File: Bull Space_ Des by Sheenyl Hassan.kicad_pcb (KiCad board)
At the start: 2 copper layers, 45 x 77 mm, 36 parts, among them IC1 TEENSY_4.0, IC2 XB24CZ7PIT-004, J1 Screw_Terminal_01x06, Q1 AOI21357, Q2 2N7002, Q3 2N7002, Q4 2N7002, Q5 AOI21357, U1 VXO7803-1000, U2 Flight-Computer_Adafruit_GPS_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

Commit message: Checked Parts
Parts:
- moved D1 3.98 mm to (91.3, 66.8)
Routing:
- net Net-(D1-Pad4): track 12.3 -> 16.7 mm
- net LED-R: track 30.9 -> 35.1 mm
- net LED-G: track 31.5 -> 35.7 mm
- net LED-B: track 32.1 -> 36.3 mm
- net Net-(D1-Pad2): track 12.0 -> 15.1 mm
- net Net-(D1-Pad3): track 14.5 -> 17.5 mm
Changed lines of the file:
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@@
   )
   (footprint "LED_THT:LED_D5.0mm-4_RGB_Staggered_Pins" (layer "F.Cu")
-    (at 95.16 67.61)
+    (at 91.26 66.81)
     (descr "LED, diameter 5.0mm, 4 pins, WP154A4, https://www.kingbright.com/attachments/file/psearch/000/00/00/L-154A4SUREQBFZGEW(Ver.11A).pdf")
     (tags "rgb led")
@@
   (gr_line (start 72 64) (end 72 141) (layer "Edge.Cuts") (width 0.1))
   (gr_line (start 116.75 141) (end 72 141) (layer "Edge.Cuts") (width 0.1))
-  (segment (start 109.098 74.214) (end 106.304 71.42) (width 0.25) (layer "F.Cu") (net 1))
-  (segment (start 109.098 75.3335) (end 109.098 74.214) (width 0.25) (layer "F.Cu") (net 1))
-  (segment (start 106.304 71.42) (end 102.272 71.42) (width 0.25) (layer "F.Cu") (net 1))
-  (segment (start 102.272 71.42) (end 99.986 69.134) (width 0.25) (layer "F.Cu") (net 1))
-  (segment (start 107.16 73.292) (end 105.796 71.928) (width 0.25) (layer "F.Cu") (net 2))
-  (segment (start 105.796 71.928) (end 100.462 71.928) (width 0.25) (layer "F.Cu") (net 2))
-  (segment (start 100.462 71.928) (end 98.462 69.928) (width 0.25) (layer "F.Cu") (net 2))
-  (segment (start 107.16 75.3335) (end 107.16 73.292) (width 0.25) (layer "F.Cu") (net 2))
-  (segment (start 98.462 69.928) (end 98.462 67.61) (width 0.25) (layer "F.Cu") (net 2))
-  (segment (start 105.26 73.424) (end 104.272 72.436) (width 0.25) (layer "F.Cu") (net 3))
-  (segment (start 104.272 72.436) (end 100.24 72.436) (width 0.25) (layer "F.Cu") (net 3))
-  (segment (start 105.26 75.3335) (end 105.26 73.424) (width 0.25) (layer "F.Cu") (net 3))
-  (segment (start 100.24 72.436) (end 96.938 69.134) (width 0.25) (layer "F.Cu") (net 3))
+  (segment (start 96.086 68.334) (end 96.086 69.606792) (width 0.25) (layer "F.Cu") (net 1))
+  (segment (start 96.086 69.606792) (end 96.744829 70.265621) (width 0.25) (layer "F.Cu") (net 1))
+  (segment (start 104.030121 70.265621) (end 109.098 75.3335) (width 0.25) (layer "F.Cu") (net 1))
+  (segment (start 96.744829 70.265621) (end 104.030121 70.265621) (width 0.25) (layer "F.Cu") (net 1))
+  (segment (start 94.562 66.81) (end 94.562 69.222282) (width 0.25) (layer "F.Cu") (net 2))
+  (segment (start 96.054859 70.715141) (end 102.541641 70.715141) (width 0.25) (layer "F.Cu") (net 2))
+  (segment (start 102.541641 70.715141) (end 107.16 75.3335) (width 0.25) (layer "F.Cu") (net 2))
+  (segment (start 94.562 69.222282) (end 96.054859 70.715141) (width 0.25) (layer "F.Cu") (net 2))
+  (segment (start 101.2365 71.31) (end 105.26 75.3335) (width 0.25) (layer "F.Cu") (net 3))
+  (segment (start 93.038 68.334) (end 96.014 71.31) (width 0.25) (layer "F.Cu") (net 3))
+  (segment (start 96.014 71.31) (end 101.2365 71.31) (width 0.25) (layer "F.Cu") (net 3))
   (segment (start 81.31 80.46) (end 81.66 80.11) (width 0.25) (layer "F.Cu") (net 6))
   (segment (start 83.388 86.35) (end 83.444 86.406) (width 0.25) (layer "F.Cu") (net 6))
@@
   (segment (start 106.4625 118.3275) (end 106.68 118.11) (width 1.5) (layer "F.Cu") (net 29))
   (segment (start 99.7 126.3875) (end 99.7 121.4975) (width 0.5) (layer "F.Cu") (net 29))
-  (segment (start 105.26 81.276997) (end 92.673006 93.863991) (width 0.25) (layer "F.Cu") (net 30))
-  (segment (start 91.813991 93.863991) (end 91.06 93.11) (width 0.25) (layer "F.Cu") (net 30))
-  (segment (start 91.06 93.11) (end 91.06 88.05) (width 0.25) (layer "F.Cu") (net 30))
-  (segment (start 92.673006 93.863991) (end 91.813991 93.863991) (width 0.25) (layer "F.Cu") (net 30))
-  (segment (start 105.26 77.1585) (end 105.26 81.276997) (width 0.25) (layer "F.Cu") (net 30))
+  (segment (start 94.487604 95.41096) (end 91.732396 95.41096) (width 0.25) (layer "F.Cu") (net 30))
+  (segment (start 105.26 84.638564) (end 94.487604 95.41096) (width 0.25) (layer "F.Cu") (net 30))
+  (segment (start 91.06 94.738564) (end 91.06 88.05) (width 0.25) (layer "F.Cu") (net 30))
+  (segment (start 91.732396 95.41096) (end 91.06 94.738564) (width 0.25) (layer "F.Cu") (net 30))
   (segment (start 91.06 88.05) (end 88.78 85.77) (width 0.25) (layer "F.Cu") (net 30))
+  (segment (start 105.26 77.1585) (end 105.26 84.638564) (width 0.25) (layer "F.Cu") (net 30))
+  (segment (start 107.16 77.1585) (end 107.16 83.374282) (width 0.25) (layer "F.Cu") (net 31))
+  (segment (start 91.546198 95.86048) (end 90.61048 94.924762) (width 0.25) (layer "F.Cu") (net 31))
+  (segment (start 107.16 83.374282) (end 94.673802 95.86048) (width 0.25) (layer "F.Cu") (net 31))
+  (segment (start 90.61048 94.924762) (end 90.61048 90.14048) (width 0.25) (layer "F.Cu") (net 31))
+  (segment (start 94.673802 95.86048) (end 91.546198 95.86048) (width 0.25) (layer "F.Cu") (net 31))
   (segment (start 90.61048 90.14048) (end 88.78 88.31) (width 0.25) (layer "F.Cu") (net 31))
-  (segment (start 107.16 77.1585) (end 107.16 80.012714) (width 0.25) (layer "F.Cu") (net 31))
-  (segment (start 91.627794 94.313511) (end 90.61048 93.296197) (width 0.25) (layer "F.Cu") (net 31))
-  (segment (start 92.859203 94.313511) (end 91.627794 94.313511) (width 0.25) (layer "F.Cu") (net 31))
-  (segment (start 90.61048 93.296197) (end 90.61048 90.14048) (width 0.25) (layer "F.Cu") (net 31))
-  (segment (start 107.16 80.012714) (end 92.859203 94.313511) (width 0.25) (layer "F.Cu") (net 31))
+  (segment (start 109.098 82.072) (end 94.86 96.31) (width 0.25) (layer "F.Cu") (net 32))
+  (segment (start 109.098 77.1585) (end 109.098 82.072) (width 0.25) (layer "F.Cu") (net 32))
+  (segment (start 94.86 96.31) (end 91.36 96.31) (width 0.25) (layer "F.Cu") (net 32))
   (segment (start 90.16096 92.23096) (end 88.78 90.85) (width 0.25) (layer "F.Cu") (net 32))
-  (segment (start 109.098 78.710431) (end 93.0454 94.763031) (width 0.25) (layer "F.Cu") (net 32))
-  (segment (start 109.098 77.1585) (end 109.098 78.710431) (width 0.25) (layer "F.Cu") (net 32))
-  (segment (start 93.0454 94.763031) (end 91.441597 94.763031) (width 0.25) (layer "F.Cu") (net 32))
-  (segment (start 90.16096 93.482394) (end 90.16096 92.23096) (width 0.25) (layer "F.Cu") (net 32))
-  (segment (start 91.441597 94.763031) (end 90.16096 93.482394) (width 0.25) (layer "F.Cu") (net 32))
+  (segment (start 90.16096 95.11096) (end 90.16096 92.23096) (width 0.25) (layer "F.Cu") (net 32))
+  (segment (start 91.36 96.31) (end 90.16096 95.11096) (width 0.25) (layer "F.Cu") (net 32))
   (segment (start 109.54 112.982228) (end 107.047772 110.49) (width 0.5) (layer "F.Cu") (net 62))
   (segment (start 103.92 110.2725) (end 106.4625 110.2725) (width 1.5) (layer "F.Cu") (net 62))

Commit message: Last Ground Fix
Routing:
- net GND: track 24.3 -> 32.9 mm, vias 2 -> 3
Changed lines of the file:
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@@
   (via (at 96.66 119.11) (size 0.8) (drill 0.4) (layers "F.Cu" "B.Cu") (net 6))
   (via (at 102.86 128.71) (size 0.8) (drill 0.4) (layers "F.Cu" "B.Cu") (net 6))
+  (via (at 99.76 95.51) (size 0.8) (drill 0.4) (layers "F.Cu" "B.Cu") (net 6))
+  (segment (start 92.24926 92.84098) (end 97.09098 92.84098) (width 0.5) (layer "B.Cu") (net 6))
+  (segment (start 97.09098 92.84098) (end 99.76 95.51) (width 0.5) (layer "B.Cu") (net 6))
   (segment (start 96.66 119.11) (end 96.66 122.51) (width 0.25) (layer "B.Cu") (net 6))
   (segment (start 96.66 122.51) (end 102.86 128.71) (width 0.25) (layer "B.Cu") (net 6))

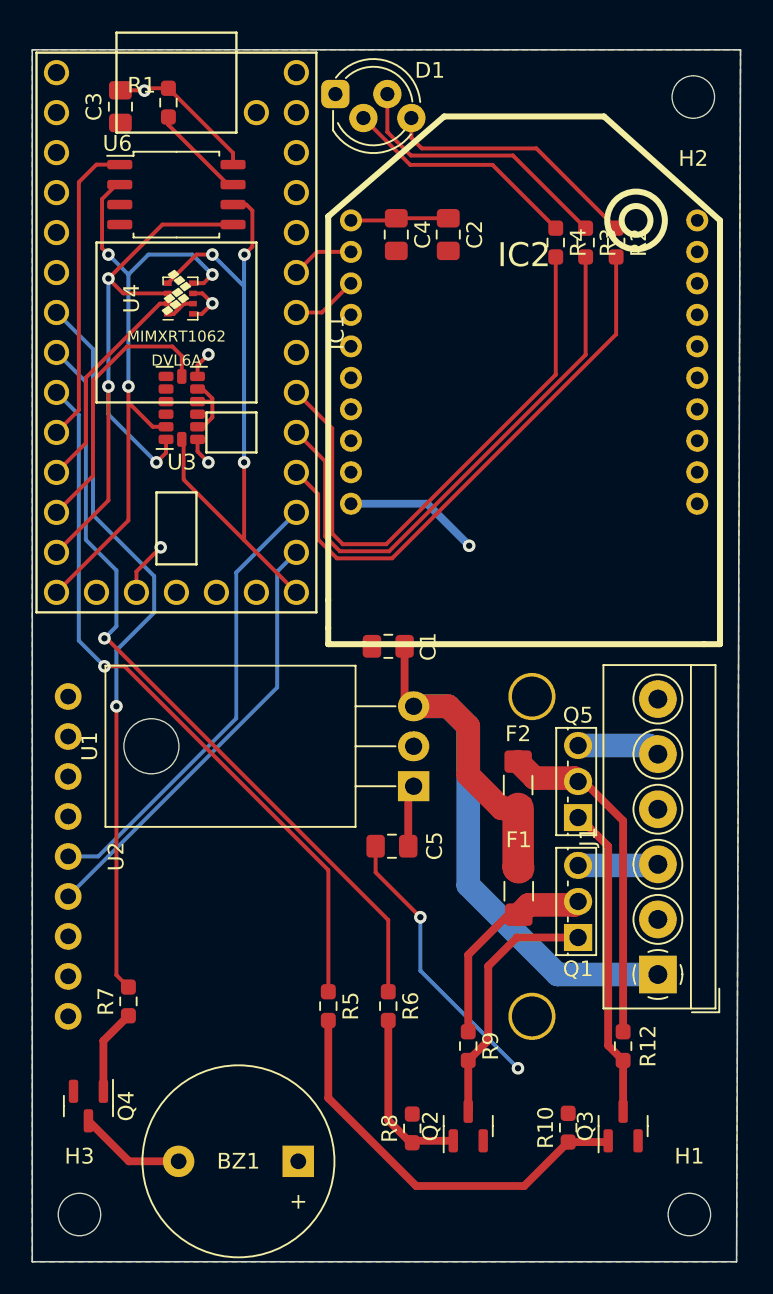
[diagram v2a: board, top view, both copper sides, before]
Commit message: Added UB SEDS Logo
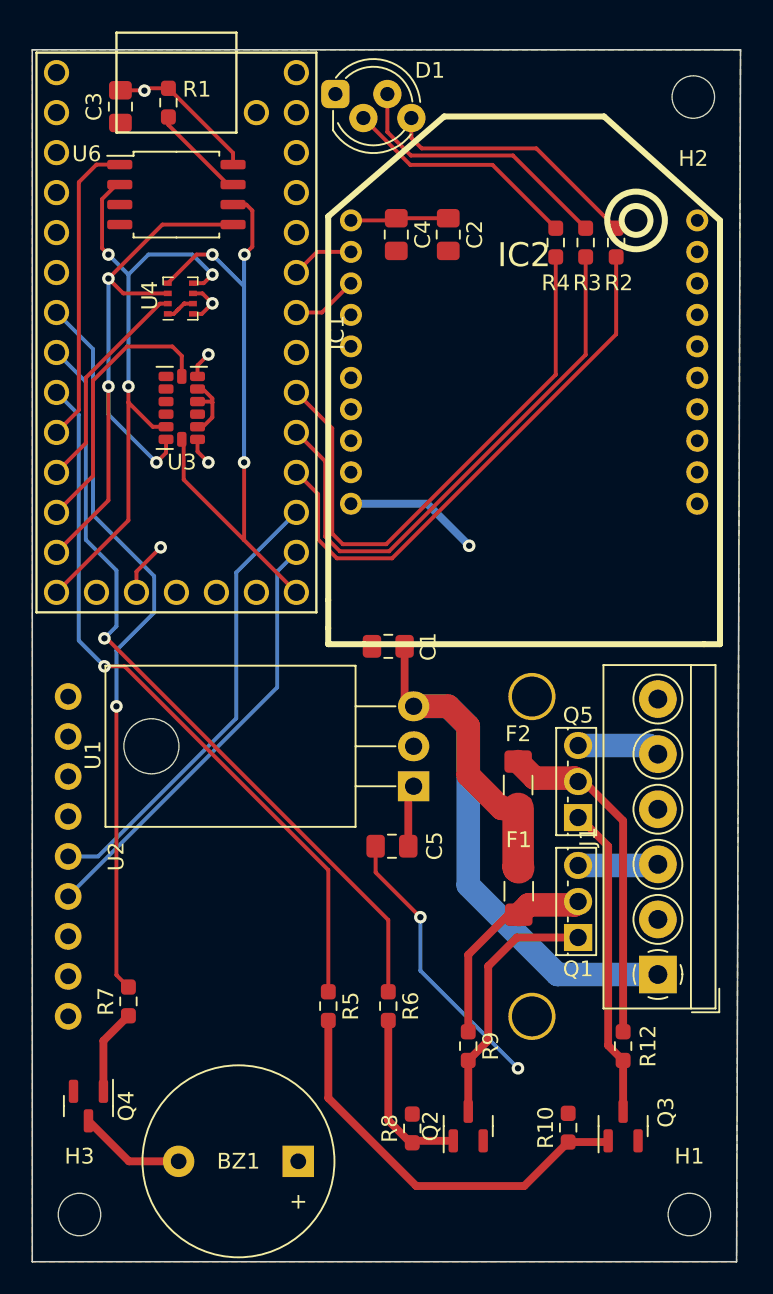
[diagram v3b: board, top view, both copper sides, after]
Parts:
- added G1: UB-SEDS-Logo, Flight Computer:SEDS_logo_soldermask, F.Cu at (101.3, 138.6)
- U3: value ADXL343 -> ADXL345

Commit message: Add files via upload
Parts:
- removed G1: UB-SEDS-Logo, Flight Computer:SEDS_logo_soldermask
- added G***: LOGO, misc diy:Seds logo v2, F.Cu at (107.3, 95.5)

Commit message: Revert "Add files via upload"
This reverts commit a89c25e643e2f36197d76d802668cdfff43c7fec.
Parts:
- removed G***: LOGO, misc diy:Seds logo v2
- added G1: UB-SEDS-Logo, Flight Computer:SEDS_logo_soldermask, F.Cu at (101.3, 138.6)
